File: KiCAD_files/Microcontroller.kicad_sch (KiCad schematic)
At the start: 59 parts, among them J403 RJE721881411, J404 RJE721881411, U401 OwnTech_SPIN, U402 TCAN334GDR, U405 LTC2850xS8, U406 MCP6487T-E/SN

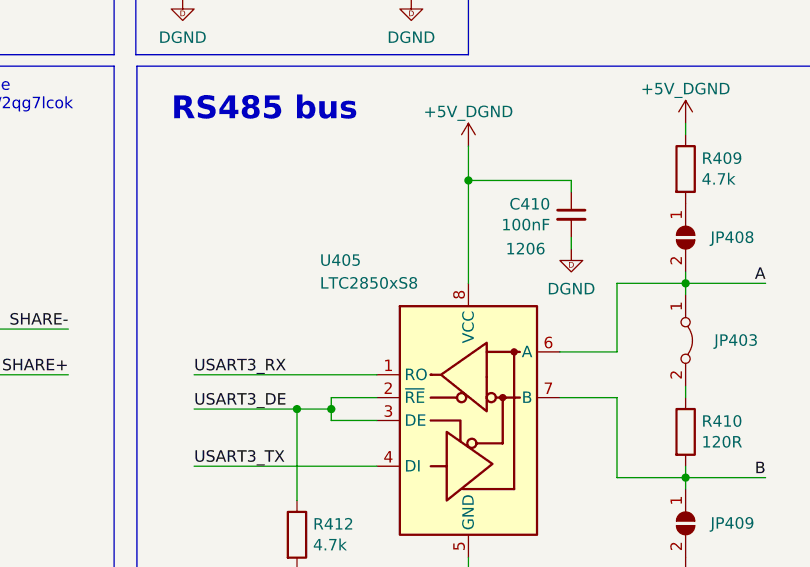
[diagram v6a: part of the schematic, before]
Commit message: LTC2850CS8#PBF is now MAX33046EASA+T
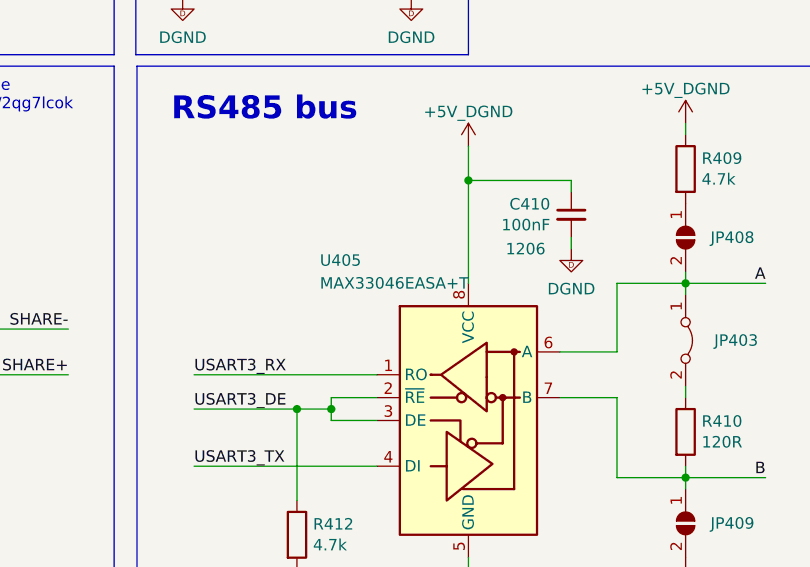
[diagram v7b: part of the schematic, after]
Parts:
- U405: value LTC2850xS8 -> MAX33046EASA+T; manf# LTC2850CS8#PBF -> MAX33046EASA+T
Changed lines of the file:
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@@
       (effects (font (size 1.27 1.27)) (justify left))
     )
-    (property "Value" "LTC2850xS8" (at 223.52 144.78 0)
+    (property "Value" "MAX33046EASA+T" (at 223.52 144.78 0)
       (effects (font (size 1.27 1.27)) (justify left))
     )
@@
       (effects (font (size 1.27 1.27)) hide)
     )
-    (property "manf#" "LTC2850CS8#PBF" (at 240.03 160.02 0)
+    (property "manf#" "MAX33046EASA+T" (at 240.03 160.02 0)
       (effects (font (size 1.27 1.27)) hide)
     )

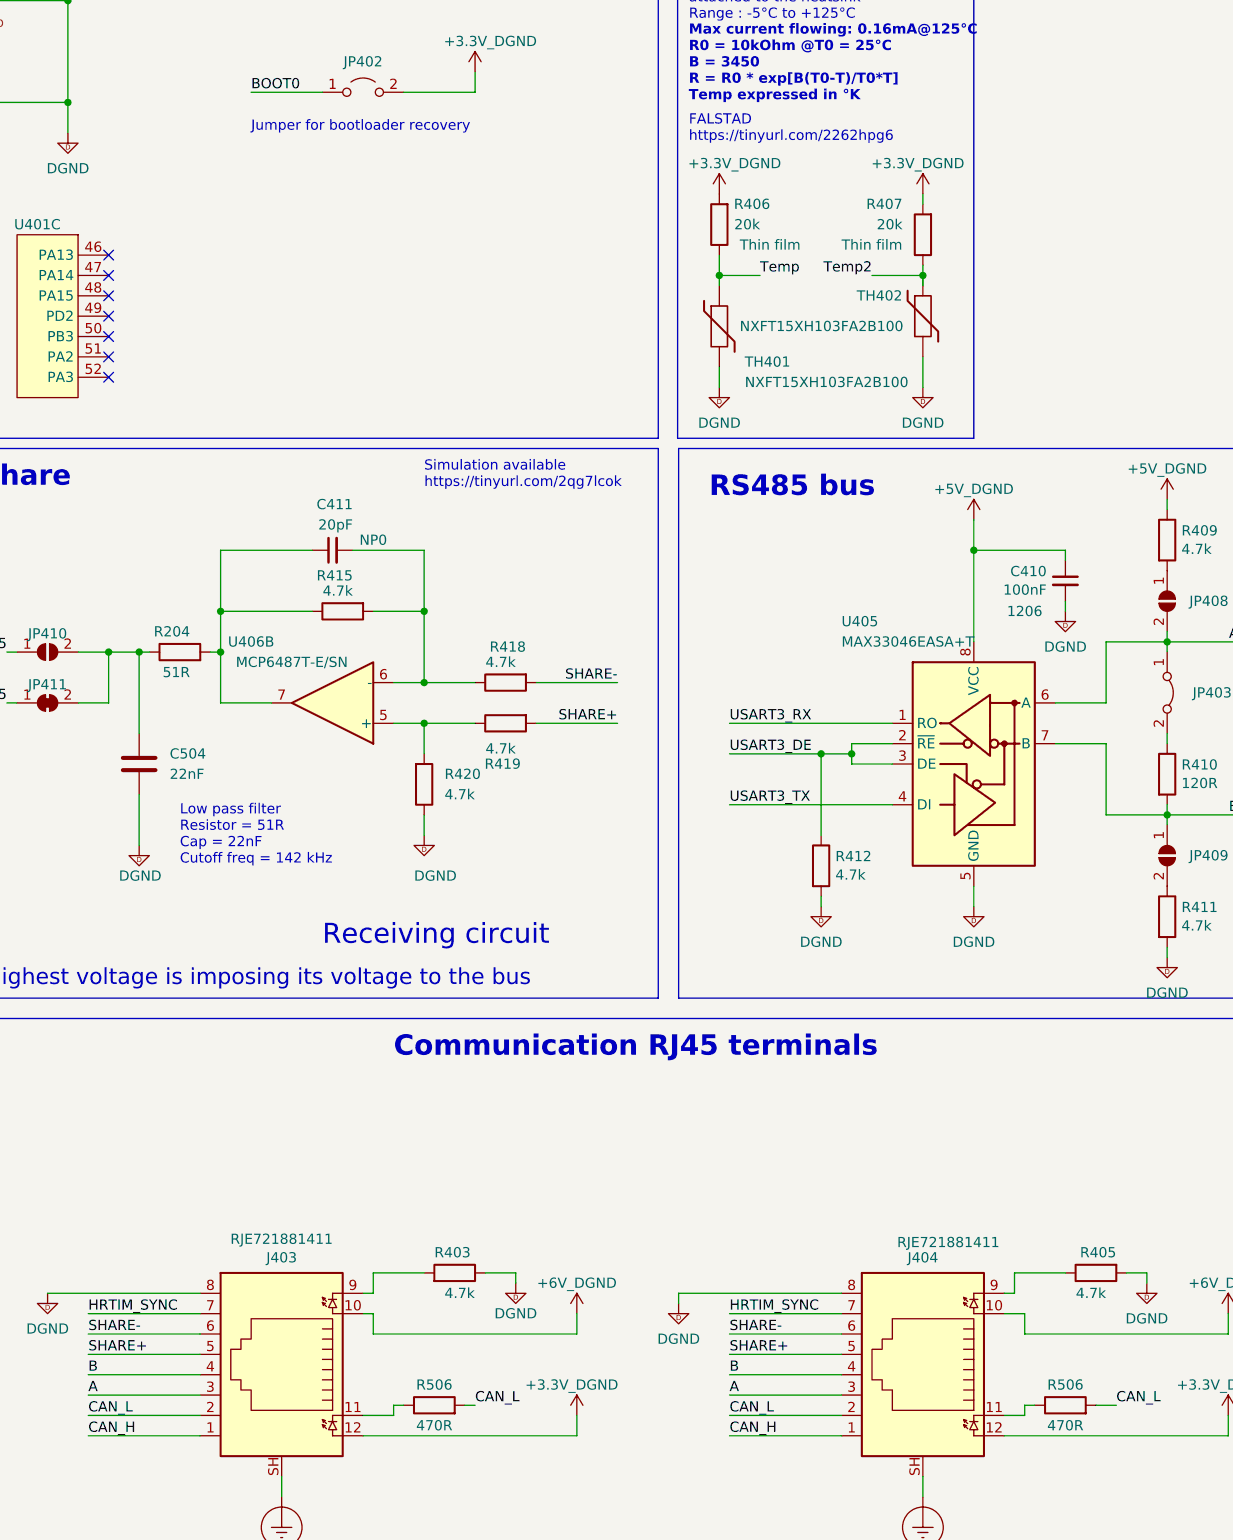
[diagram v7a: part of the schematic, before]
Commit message: Added BOOT0 pull down - Checked PMOS rerouting Suppress thermal reliefs on LEG1 high side. Suppress copper finger below inductors. Moved resistors close to OAmp to make silkscreen better
Signed-off-by: Jean Alinei <jean.alinei@laas.fr>
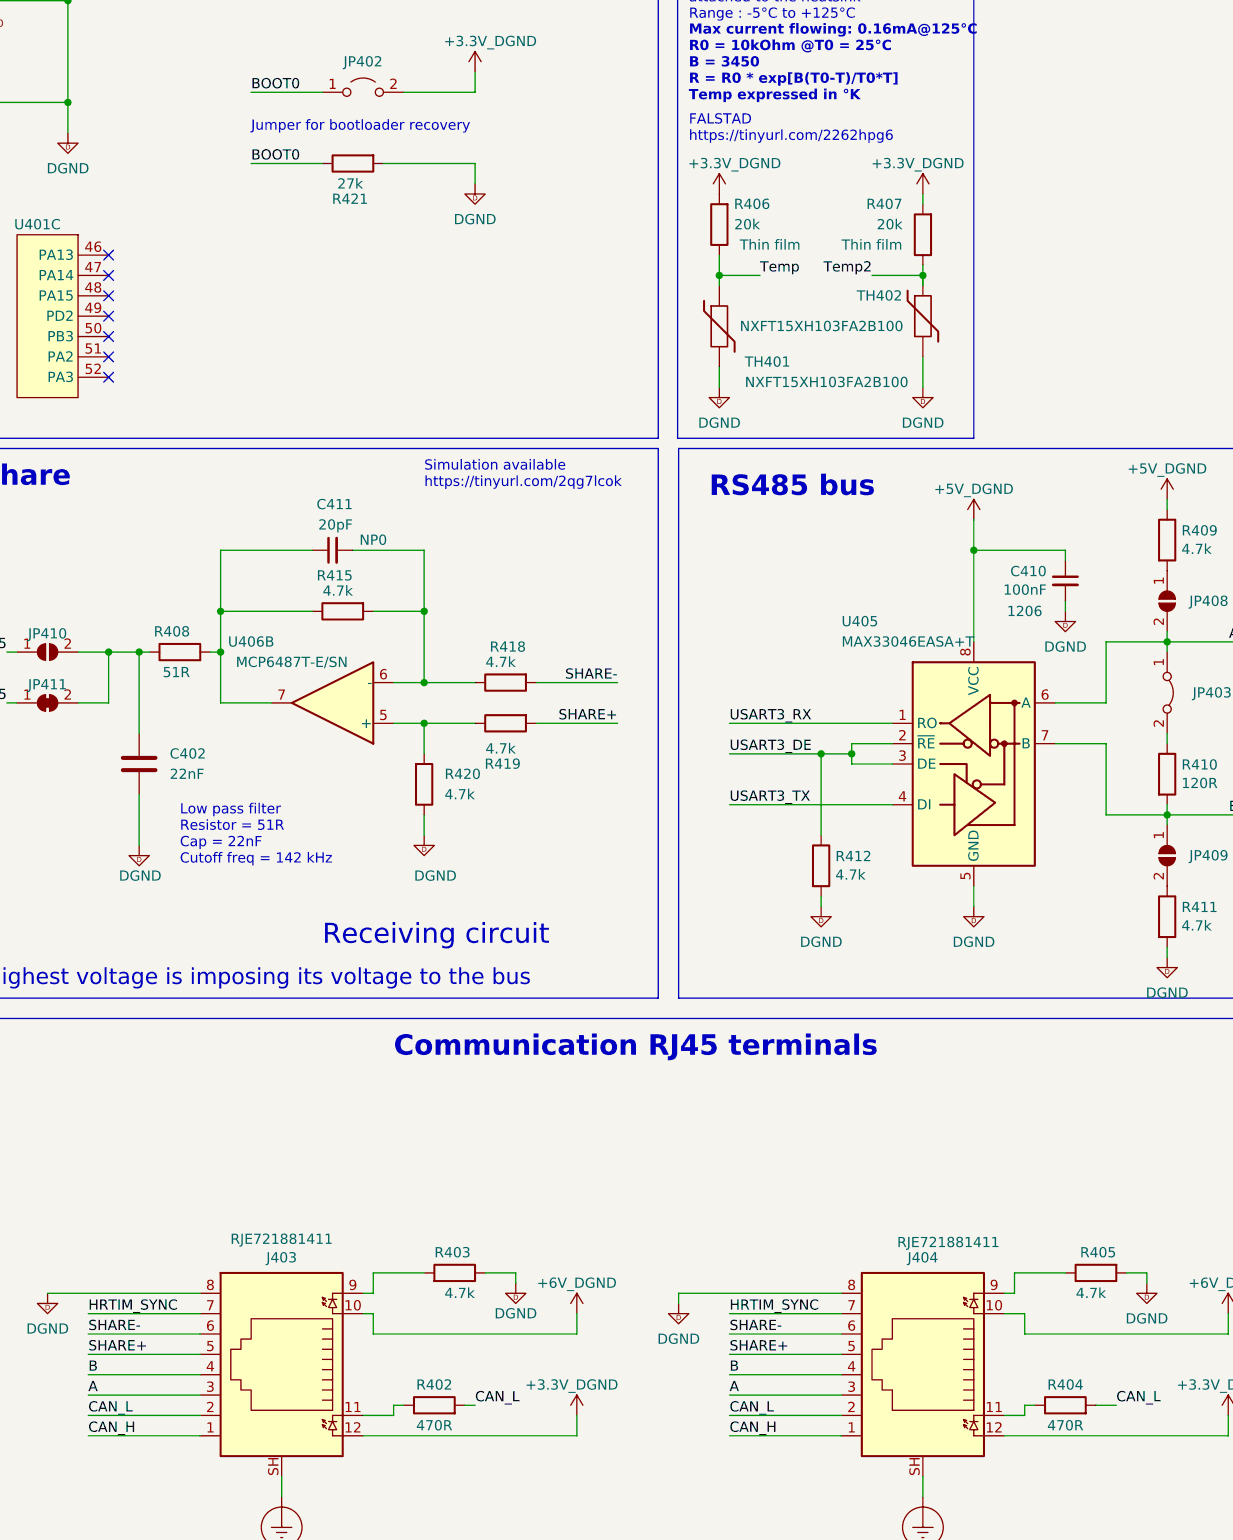
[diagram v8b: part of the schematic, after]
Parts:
- added R421: 27k, Footprints:R_0805_2012Metric, symbol Device:R
- renumbered C504 to C402, R506 to R402, R506 to R404, R204 to R408
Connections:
- net BOOT0: now also R421.1
- net DGND: now also R421.2
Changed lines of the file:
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@@
     (stroke (width 0) (type default))
   )
+  (wire (pts (xy 177.8 85.09) (xy 177.8 87.63))
+    (stroke (width 0) (type default))
+  )
   (wire (pts (xy 233.68 88.9) (xy 233.68 90.17))
     (stroke (width 0) (type default))
@@
     (stroke (width 0) (type default))
   )
+  (wire (pts (xy 166.37 85.09) (xy 177.8 85.09))
+    (stroke (width 0) (type default))
+  )
   (wire (pts (xy 127 52.07) (xy 127 64.77))
     (stroke (width 0) (type default))
@@
     (stroke (width 0) (type default))
   )
+  (wire (pts (xy 149.86 85.09) (xy 158.75 85.09))
+    (stroke (width 0) (type default))
+  )
   (wire (pts (xy 256.54 152.4) (xy 256.54 144.78))
     (stroke (width 0) (type default))
@@
     (effects (font (size 1.27 1.27)) (justify right bottom))
   )
+  (label "BOOT0" (at 149.86 85.09 0) (fields_autoplaced)
+    (effects (font (size 1.27 1.27)) (justify left bottom))
+  )
   (label "FDCAN2_{TX}" (at 81.28 102.87 90) (fields_autoplaced)
     (effects (font (size 1.27 1.27)) (justify left bottom))
@@
   (symbol (lib_id "Device:R") (at 172.72 240.03 90) (unit 1)
     (in_bom yes) (on_board yes) (dnp no)
-    (property "Reference" "R506" (at 172.72 237.49 90)
+    (property "Reference" "R402" (at 172.72 237.49 90)
       (effects (font (size 1.27 1.27)))
     )
@@
     (instances
       (project "Power"
-        (path "/8d0c1d66-35ef-4a53-a28f-436a11b54f42/bce1534c-362e-45ed-a9dd-a44d6954485a"
-          (reference "R506") (unit 1)
-        )
         (path "/8d0c1d66-35ef-4a53-a28f-436a11b54f42/122c01f4-f23e-4db0-9503-7261d96dc78b"
           (reference "R402") (unit 1)
@@
   (symbol (lib_id "Symbols:+6V_DGND") (at 190.5 228.6 0) (unit 1)
     (in_bom no) (on_board no) (dnp no) (fields_autoplaced)
-    (property "Reference" "#PWR010" (at 192.278 228.6 90)
+    (property "Reference" "#PWR016" (at 192.278 228.6 90)
       (effects (font (size 1.27 1.27)) hide)
     )
@@
     (instances
       (project "Power"
-        (path "/8d0c1d66-35ef-4a53-a28f-436a11b54f42"
-          (reference "#PWR010") (unit 1)
-        )
         (path "/8d0c1d66-35ef-4a53-a28f-436a11b54f42/122c01f4-f23e-4db0-9503-7261d96dc78b"
           (reference "#PWR016") (unit 1)
@@
   (symbol (lib_id "Device:C") (at 135.89 160.02 0) (unit 1)
     (in_bom yes) (on_board yes) (dnp no)
-    (property "Reference" "C504" (at 139.7 158.75 0)
+    (property "Reference" "C402" (at 139.7 158.75 0)
       (effects (font (size 1.27 1.27)) (justify left))
     )
@@
     (instances
       (project "Power"
-        (path "/8d0c1d66-35ef-4a53-a28f-436a11b54f42/bce1534c-362e-45ed-a9dd-a44d6954485a"
-          (reference "C504") (unit 1)
-        )
         (path "/8d0c1d66-35ef-4a53-a28f-436a11b54f42/122c01f4-f23e-4db0-9503-7261d96dc78b"
           (reference "C402") (unit 1)
@@
   (symbol (lib_id "Device:R") (at 140.97 146.05 90) (unit 1)
     (in_bom yes) (on_board yes) (dnp no)
-    (property "Reference" "R204" (at 142.24 143.51 90)
+    (property "Reference" "R408" (at 142.24 143.51 90)
       (effects (font (size 1.27 1.27)) (justify left))
     )
@@
     (instances
       (project "Power"
-        (path "/8d0c1d66-35ef-4a53-a28f-436a11b54f42/b9592210-62fd-48e0-8447-67f645d7d247"
-          (reference "R204") (unit 1)
-        )
-        (path "/8d0c1d66-35ef-4a53-a28f-436a11b54f42/4a11142e-1c8b-45f6-8828-f013379f9fc1"
-          (reference "R304") (unit 1)
-        )
         (path "/8d0c1d66-35ef-4a53-a28f-436a11b54f42/122c01f4-f23e-4db0-9503-7261d96dc78b"
           (reference "R408") (unit 1)
@@
     )
   )
+  (symbol (lib_id "Symbols:DGND") (at 177.8 87.63 0) (unit 1)
+    (in_bom yes) (on_board yes) (dnp no) (fields_autoplaced)
+    (property "Reference" "#PWR0407" (at 177.8 93.98 0)
+      (effects (font (size 1.27 1.27)) hide)
+    )
+    (property "Value" "DGND" (at 177.8 92.075 0)
+      (effects (font (size 1.27 1.27)))
+    )
+    (property "Footprint" "" (at 177.8 87.63 0)
+      (effects (font (size 1.27 1.27)) hide)
+    )
+    (property "Datasheet" "" (at 177.8 87.63 0)
+      (effects (font (size 1.27 1.27)) hide)
+    )
+    (pin "1")
+    (instances
+      (project "Power"
+        (path "/8d0c1d66-35ef-4a53-a28f-436a11b54f42/122c01f4-f23e-4db0-9503-7261d96dc78b"
+          (reference "#PWR0407") (unit 1)
+        )
+      )
+    )
+  )
   (symbol (lib_id "Jumper:Jumper_2_Open") (at 163.83 76.2 0) (unit 1)
     (in_bom yes) (on_board yes) (dnp no)
@@
   (symbol (lib_id "Symbols:+6V_DGND") (at 271.78 228.6 0) (unit 1)
     (in_bom no) (on_board no) (dnp no) (fields_autoplaced)
-    (property "Reference" "#PWR010" (at 273.558 228.6 90)
+    (property "Reference" "#PWR017" (at 273.558 228.6 90)
       (effects (font (size 1.27 1.27)) hide)
     )
@@
     (instances
       (project "Power"
-        (path "/8d0c1d66-35ef-4a53-a28f-436a11b54f42"
-          (reference "#PWR010") (unit 1)
-        )
         (path "/8d0c1d66-35ef-4a53-a28f-436a11b54f42/122c01f4-f23e-4db0-9503-7261d96dc78b"
           (reference "#PWR017") (unit 1)
@@
     )
   )
+  (symbol (lib_id "Device:R") (at 162.56 85.09 90) (mirror x) (unit 1)
+    (in_bom yes) (on_board yes) (dnp no)
+    (property "Reference" "R421" (at 164.465 89.535 90)
+      (effects (font (size 1.27 1.27)) (justify left))
+    )
+    (property "Value" "27k" (at 163.83 87.63 90)
+      (effects (font (size 1.27 1.27)) (justify left))
+    )
+    (property "Footprint" "Footprints:R_0805_2012Metric" (at 162.56 83.312 90)
+      (effects (font (size 1.27 1.27)) hide)
+    )
+    (property "Datasheet" "${KIPRJMOD}\\datasheet\\cr-1858361.pdf" (at 162.56 85.09 0)
+      (effects (font (size 1.27 1.27)) hide)
+    )
+    (property "DNP" "" (at 162.56 85.09 0)
+      (effects (font (size 1.27 1.27)) hide)
+    )
+    (property "manf#" "CR0805-FX-4701ELF" (at 162.56 85.09 0)
+      (effects (font (size 1.27 1.27)) hide)
+    )
+    (property "Functional Block" "Communication" (at 162.56 85.09 0)
+      (effects (font (size 1.27 1.27)) hide)
+    )
+    (property "Metal content" "NiCr" (at 162.56 85.09 0)
+      (effects (font (size 1.27 1.27)) hide)
+    )
+    (property "Subfunction" "Analog bus" (at 162.56 85.09 0)
+      (effects (font (size 1.27 1.27)) hide)
+    )
+    (property "Package" "0805" (at 162.56 85.09 0)
+      (effects (font (size 1.27 1.27)) hide)
+    )
+    (property "Technology" "Thick film" (at 162.56 85.09 0)
+      (effects (font (size 1.27 1.27)) hide)
+    )
+    (pin "1")
+    (pin "2")
+    (instances
+      (project "Power"
+        (path "/8d0c1d66-35ef-4a53-a28f-436a11b54f42/122c01f4-f23e-4db0-9503-7261d96dc78b"
+          (reference "R421") (unit 1)
+        )
+      )
+    )
+  )
   (symbol (lib_id "Symbols:DGND") (at 223.52 27.94 0) (unit 1)
     (in_bom yes) (on_board yes) (dnp no) (fields_autoplaced)
@@
   (symbol (lib_id "Device:R") (at 251.46 240.03 90) (unit 1)
     (in_bom yes) (on_board yes) (dnp no)
-    (property "Reference" "R506" (at 251.46 237.49 90)
+    (property "Reference" "R404" (at 251.46 237.49 90)
       (effects (font (size 1.27 1.27)))
     )
@@
     (instances
       (project "Power"
-        (path "/8d0c1d66-35ef-4a53-a28f-436a11b54f42/bce1534c-362e-45ed-a9dd-a44d6954485a"
-          (reference "R506") (unit 1)
-        )
         (path "/8d0c1d66-35ef-4a53-a28f-436a11b54f42/122c01f4-f23e-4db0-9503-7261d96dc78b"
           (reference "R404") (unit 1)
